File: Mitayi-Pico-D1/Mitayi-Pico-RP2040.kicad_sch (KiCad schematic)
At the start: 57 parts, among them J1 EXP8, J10 GND, J2 USB-C-2.0, J3 Header-1, J4 Header-2, J5 SWD, J6 USB_B_Micro, J7 VBUS, J8 DM, J9 DP, SW1 UK-B0273-SP25Y, SW2 UK-B0273-SP25Y, U1 W25Q32JVSSIQ, U2 MIC5219-3.3YM5, U3 RP2040, Y1 YIC-12M20P2/XT324-10/10

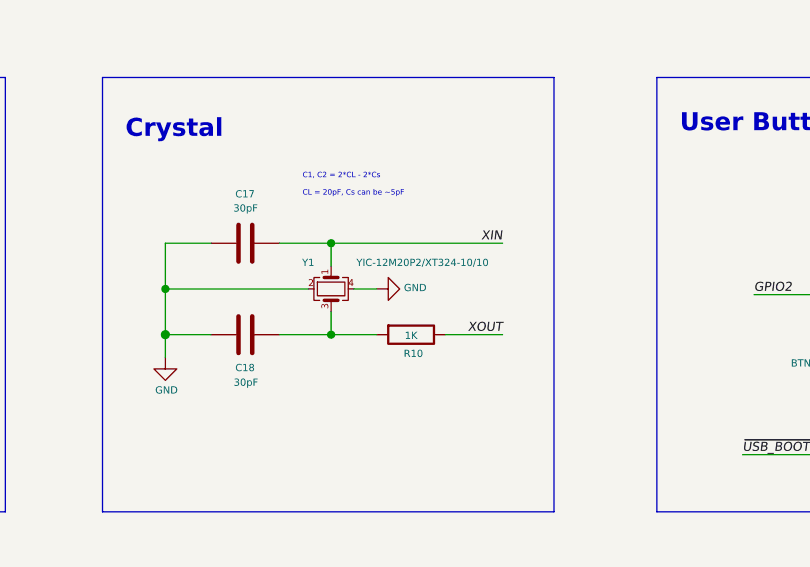
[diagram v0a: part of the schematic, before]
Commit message: Updated `runDRC()`
- Updated `runDRC()`.
  - It now checks how many voilations were found in the DRC report and print them.
  - If violations are found, the user will be prompted to continue or exit the app.
  - The export log won't be saved if the user chooses to exit. The report will still be saved.
  - `pcb_drc` command execcution will be set to false if the user chooses to continue with DRC errors.
- New Version 🆕 `0.1.7`.
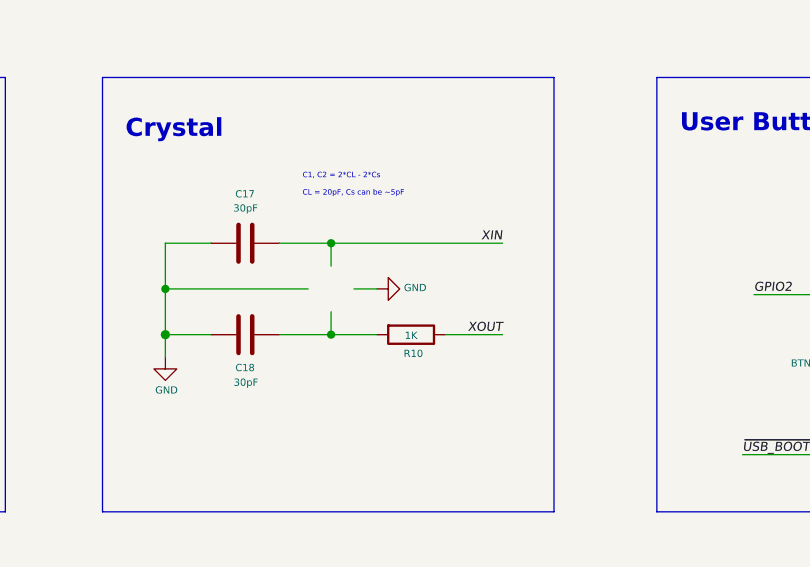
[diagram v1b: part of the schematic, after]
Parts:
- removed Y1: YIC-12M20P2/XT324-10/10, Crystal:Crystal_SMD_3225-4Pin_3.2x2.5mm, symbol Device:Crystal_GND24_Small
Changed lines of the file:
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@@
-	)
-	(symbol
-		(lib_id "Device:Crystal_GND24_Small")
-		(at 105.41 186.055 270)
-		(unit 1)
-		(exclude_from_sim no)
-		(in_bom yes)
-		(on_board yes)
-		(dnp no)
-		(property "Reference" "Y1"
-			(at 102.87 183.1338 90)
-			(effects
-				(font
-					(size 0.8 0.8)
-				)
-			)
-		)
-		(property "Value" "YIC-12M20P2/XT324-10/10"
-			(at 115.57 183.1338 90)
-			(effects
-				(font
-					(size 0.8 0.8)
-				)
-			)
-		)
-		(property "Footprint" "Crystal:Crystal_SMD_3225-4Pin_3.2x2.5mm"
-			(at 105.41 186.055 0)
-			(hide yes)
-			(effects
-				(font
-					(size 0.8 0.8)
-				)
-			)
-		)
-		(property "Datasheet" ""
-			(at 105.41 186.055 0)
-			(hide yes)
-			(effects
-				(font
-					(size 0.8 0.8)
-				)
-			)
-		)
-		(property "Description" ""
-			(at 105.41 186.055 0)
-			(hide yes)
-			(effects
-				(font
-					(size 1.27 1.27)
-				)
-			)
-		)
-		(property "MFR" "YIC"
-			(at 105.41 186.055 0)
-			(hide yes)
-			(effects
-				(font
-					(size 1.27 1.27)
-				)
-			)
-		)
-		(property "MPN" "YIC-12M20P2/XT324-10/10"
-			(at 105.41 186.055 0)
-			(hide yes)
-			(effects
-				(font
-					(size 1.27 1.27)
-				)
-			)
-		)
-		(property "Name" ""
-			(at 105.41 186.055 0)
-			(hide yes)
-			(effects
-				(font
-					(size 1.27 1.27)
-				)
-			)
-		)
-		(property "Alt MPN" ""
-			(at 105.41 186.055 0)
-			(hide yes)
-			(effects
-				(font
-					(size 1.27 1.27)
-				)
-			)
-		)
-		(pin "1"
-		)
-		(pin "2"
-		)
-		(pin "3"
-		)
-		(pin "4"
-		)
-		(instances
-			(project "Mitayi-Pico-RP2040"
-				(path "/35c47459-45a7-4753-acae-c8b47e7575e1"
-					(reference "Y1")
-					(unit 1)
-				)
-			)
-		)
 	)
 	(symbol

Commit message: Udpated
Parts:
- added Y1: YIC-12M20P2/XT324-10/10, Crystal:Crystal_SMD_3225-4Pin_3.2x2.5mm, symbol Device:Crystal_GND24_Small
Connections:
- net GND: now also Y1.2, Y1.4
- net XIN: now also Y1.1
- net at C18.1, R10.2: now also Y1.3
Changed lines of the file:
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@@
+	)
+	(symbol
+		(lib_id "Device:Crystal_GND24_Small")
+		(at 105.41 186.055 270)
+		(unit 1)
+		(exclude_from_sim no)
+		(in_bom yes)
+		(on_board yes)
+		(dnp no)
+		(property "Reference" "Y1"
+			(at 102.87 183.1338 90)
+			(effects
+				(font
+					(size 0.8 0.8)
+				)
+			)
+		)
+		(property "Value" "YIC-12M20P2/XT324-10/10"
+			(at 115.57 183.1338 90)
+			(effects
+				(font
+					(size 0.8 0.8)
+				)
+			)
+		)
+		(property "Footprint" "Crystal:Crystal_SMD_3225-4Pin_3.2x2.5mm"
+			(at 105.41 186.055 0)
+			(hide yes)
+			(effects
+				(font
+					(size 0.8 0.8)
+				)
+			)
+		)
+		(property "Datasheet" ""
+			(at 105.41 186.055 0)
+			(hide yes)
+			(effects
+				(font
+					(size 0.8 0.8)
+				)
+			)
+		)
+		(property "Description" ""
+			(at 105.41 186.055 0)
+			(hide yes)
+			(effects
+				(font
+					(size 1.27 1.27)
+				)
+			)
+		)
+		(property "MFR" "YIC"
+			(at 105.41 186.055 0)
+			(hide yes)
+			(effects
+				(font
+					(size 1.27 1.27)
+				)
+			)
+		)
+		(property "MPN" "YIC-12M20P2/XT324-10/10"
+			(at 105.41 186.055 0)
+			(hide yes)
+			(effects
+				(font
+					(size 1.27 1.27)
+				)
+			)
+		)
+		(property "Name" ""
+			(at 105.41 186.055 0)
+			(hide yes)
+			(effects
+				(font
+					(size 1.27 1.27)
+				)
+			)
+		)
+		(property "Alt MPN" ""
+			(at 105.41 186.055 0)
+			(hide yes)
+			(effects
+				(font
+					(size 1.27 1.27)
+				)
+			)
+		)
+		(pin "1"
+		)
+		(pin "2"
+		)
+		(pin "3"
+		)
+		(pin "4"
+		)
+		(instances
+			(project "Mitayi-Pico-RP2040"
+				(path "/35c47459-45a7-4753-acae-c8b47e7575e1"
+					(reference "Y1")
+					(unit 1)
+				)
+			)
+		)
 	)
 	(symbol
